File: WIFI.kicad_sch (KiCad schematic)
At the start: 34 parts, among them J4 ESP Anten, SW2 ESP_RESET, SW3 ESP_BOOT, U3 ESP32-C3, U4 W25Q32JVSS, Y2 40MHz

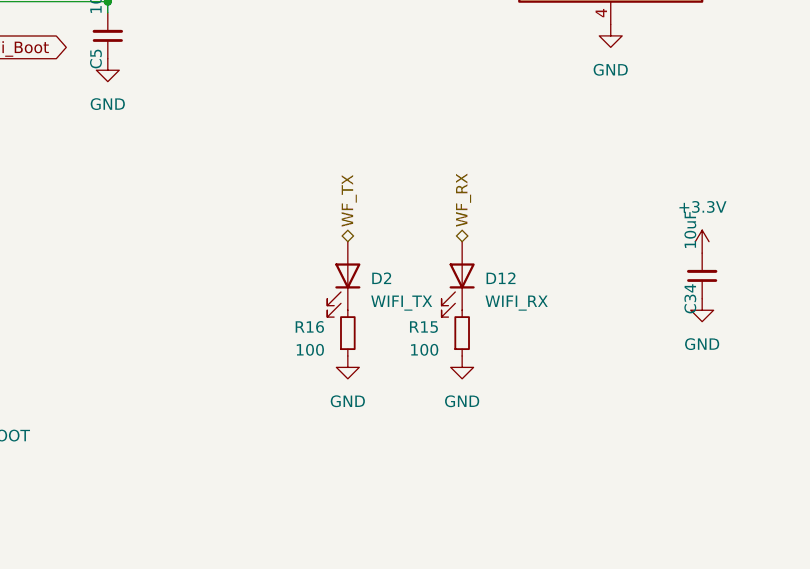
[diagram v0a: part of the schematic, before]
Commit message: Finish routing.
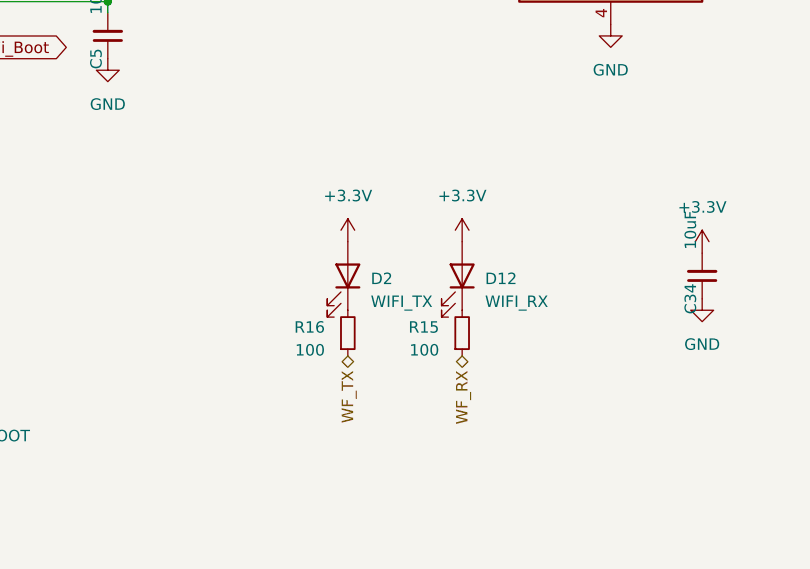
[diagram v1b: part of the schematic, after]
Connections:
- net +3.3V: now also D12.2 (A), D2.2 (A)
- net GND: no longer R15.1, R16.1
- net WF_RX: now also R15.1; no longer D12.2 (A)
- net WF_TX: now also R16.1; no longer D2.2 (A)
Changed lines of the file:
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@@
     )
   )
-  (hierarchical_label "WF_TX" (shape bidirectional) (at 189.23 134.62 90) (fields_autoplaced)
-    (effects (font (size 1.27 1.27)) (justify left))
+  (hierarchical_label "WF_TX" (shape bidirectional) (at 189.23 147.32 270) (fields_autoplaced)
+    (effects (font (size 1.27 1.27)) (justify right))
   )
   (hierarchical_label "USB_D_P" (shape bidirectional) (at 146.05 83.82 0) (fields_autoplaced)
@@
     (effects (font (size 1.27 1.27)) (justify left))
   )
-  (hierarchical_label "WF_RX" (shape bidirectional) (at 201.93 134.62 90) (fields_autoplaced)
-    (effects (font (size 1.27 1.27)) (justify left))
+  (hierarchical_label "WF_RX" (shape bidirectional) (at 201.93 147.32 270) (fields_autoplaced)
+    (effects (font (size 1.27 1.27)) (justify right))
   )
   (symbol (lib_id "Device:C_Small") (at 64.77 130.81 180) (unit 1)
@@
     )
   )
-  (symbol (lib_id "power:GND") (at 201.93 147.32 0) (mirror y) (unit 1)
-    (in_bom yes) (on_board yes) (dnp no) (fields_autoplaced)
-    (property "Reference" "#PWR059" (at 201.93 153.67 0)
-      (effects (font (size 1.27 1.27)) hide)
-    )
-    (property "Value" "GND" (at 201.93 152.4 0)
-      (effects (font (size 1.27 1.27)))
-    )
-    (property "Footprint" "" (at 201.93 147.32 0)
-      (effects (font (size 1.27 1.27)) hide)
-    )
-    (property "Datasheet" "" (at 201.93 147.32 0)
-      (effects (font (size 1.27 1.27)) hide)
-    )
-    (pin "1")
-    (instances
-      (project "GatewayPlus_V1.4"
-        (path "/6b25bb2e-e3f8-49e6-940a-fa3f985570a5/93629978-ce95-4bf7-bdaf-5ff23fa4963a"
-          (reference "#PWR059") (unit 1)
-        )
-      )
-    )
-  )
   (symbol (lib_id "Device:C_Small") (at 63.5 96.52 270) (unit 1)
     (in_bom yes) (on_board yes) (dnp no)
@@
     )
   )
-  (symbol (lib_id "power:GND") (at 189.23 147.32 0) (mirror y) (unit 1)
-    (in_bom yes) (on_board yes) (dnp no) (fields_autoplaced)
-    (property "Reference" "#PWR067" (at 189.23 153.67 0)
-      (effects (font (size 1.27 1.27)) hide)
-    )
-    (property "Value" "GND" (at 189.23 152.4 0)
-      (effects (font (size 1.27 1.27)))
-    )
-    (property "Footprint" "" (at 189.23 147.32 0)
-      (effects (font (size 1.27 1.27)) hide)
-    )
-    (property "Datasheet" "" (at 189.23 147.32 0)
-      (effects (font (size 1.27 1.27)) hide)
-    )
-    (pin "1")
-    (instances
-      (project "GatewayPlus_V1.4"
-        (path "/6b25bb2e-e3f8-49e6-940a-fa3f985570a5/93629978-ce95-4bf7-bdaf-5ff23fa4963a"
-          (reference "#PWR067") (unit 1)
+  (symbol (lib_id "power:+3.3V") (at 201.93 134.62 0) (mirror y) (unit 1)
+    (in_bom yes) (on_board yes) (dnp no) (fields_autoplaced)
+    (property "Reference" "#PWR059" (at 201.93 138.43 0)
+      (effects (font (size 1.27 1.27)) hide)
+    )
+    (property "Value" "+3.3V" (at 201.93 129.54 0)
+      (effects (font (size 1.27 1.27)))
+    )
+    (property "Footprint" "" (at 201.93 134.62 0)
+      (effects (font (size 1.27 1.27)) hide)
+    )
+    (property "Datasheet" "" (at 201.93 134.62 0)
+      (effects (font (size 1.27 1.27)) hide)
+    )
+    (pin "1")
+    (instances
+      (project "GatewayPlus_V1.4"
+        (path "/6b25bb2e-e3f8-49e6-940a-fa3f985570a5/93629978-ce95-4bf7-bdaf-5ff23fa4963a"
+          (reference "#PWR059") (unit 1)
         )
       )
@@
         )
       )
+    )
+  )
+  (symbol (lib_id "power:+3.3V") (at 189.23 134.62 0) (mirror y) (unit 1)
+    (in_bom yes) (on_board yes) (dnp no) (fields_autoplaced)
+    (property "Reference" "#PWR067" (at 189.23 138.43 0)
+      (effects (font (size 1.27 1.27)) hide)
+    )
+    (property "Value" "+3.3V" (at 189.23 129.54 0)
+      (effects (font (size 1.27 1.27)))
+    )
+    (property "Footprint" "" (at 189.23 134.62 0)
+      (effects (font (size 1.27 1.27)) hide)
+    )
+    (property "Datasheet" "" (at 189.23 134.62 0)
+      (effects (font (size 1.27 1.27)) hide)
+    )
+    (pin "1")
+    (instances
+      (project "GatewayPlus_V1.4"
+        (path "/6b25bb2e-e3f8-49e6-940a-fa3f985570a5/93629978-ce95-4bf7-bdaf-5ff23fa4963a"
+          (reference "#PWR067") (unit 1)
+        )
+      )

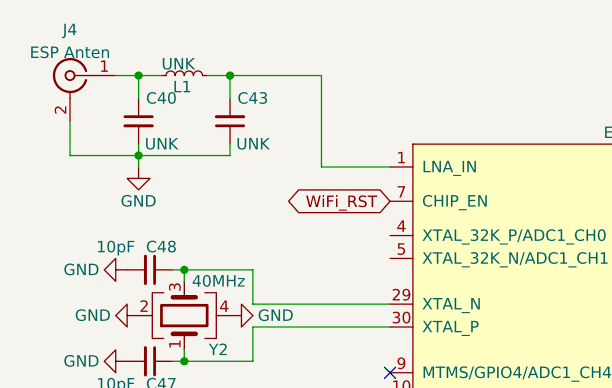
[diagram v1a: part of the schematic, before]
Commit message: Fix USB silkscreen name.
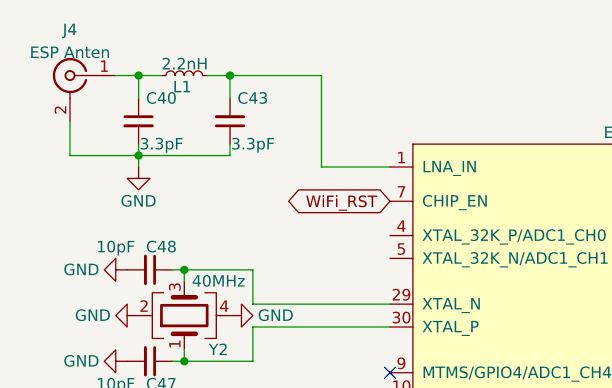
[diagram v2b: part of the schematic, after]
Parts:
- C40, C43: value UNK -> 3.3pF
- L1: value UNK -> 2.2nH
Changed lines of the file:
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@@
       (effects (font (size 1.27 1.27)) (justify right))
     )
-    (property "Value" "UNK" (at 64.77 63.5 90)
+    (property "Value" "2.2nH" (at 64.77 63.5 90)
       (effects (font (size 1.27 1.27)) (justify right))
     )
@@
       (effects (font (size 1.27 1.27)))
     )
-    (property "Value" "UNK" (at 64.77 72.39 0)
+    (property "Value" "3.3pF" (at 64.77 72.39 0)
       (effects (font (size 1.27 1.27)))
     )
@@
       (effects (font (size 1.27 1.27)))
     )
-    (property "Value" "UNK" (at 74.93 72.39 0)
-      (effects (font (size 1.27 1.27)))
-    )
+    (property "Value" "3.3pF" (at 74.93 72.39 0)
+      (effects (font (size 1.27 1.27)))
+    )
